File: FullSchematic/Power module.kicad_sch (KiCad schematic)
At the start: 1 part

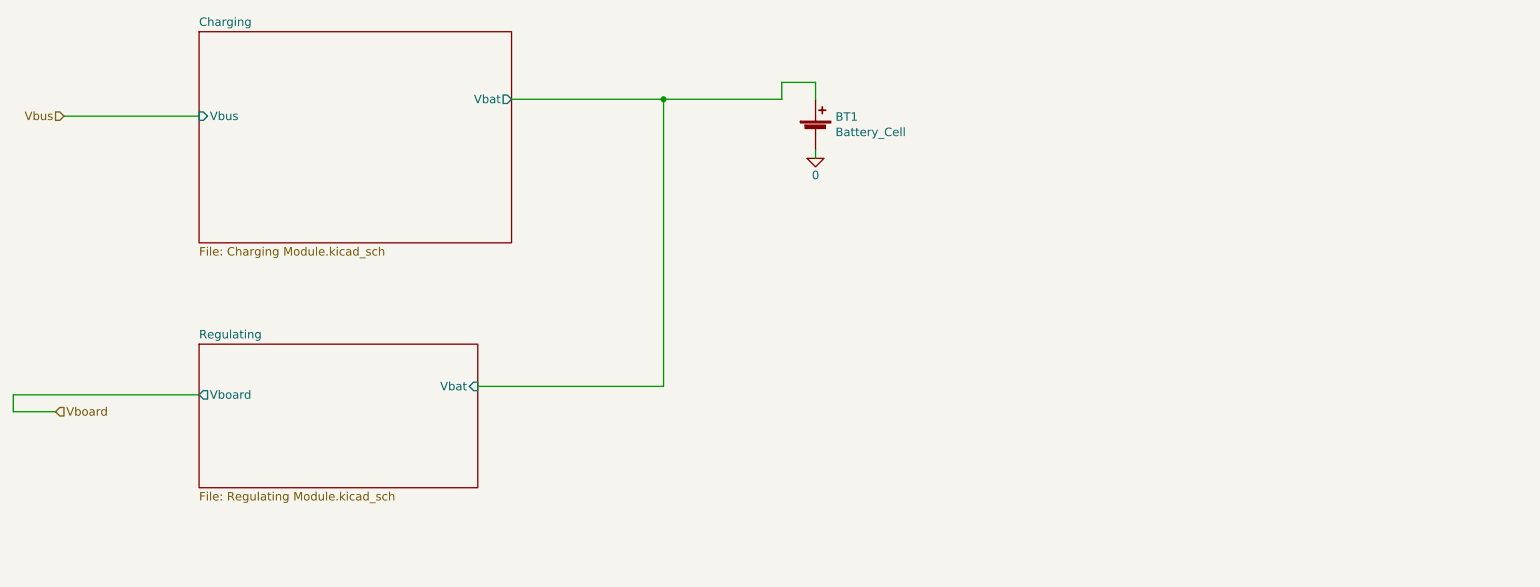
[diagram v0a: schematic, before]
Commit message: Added uvlo circuit
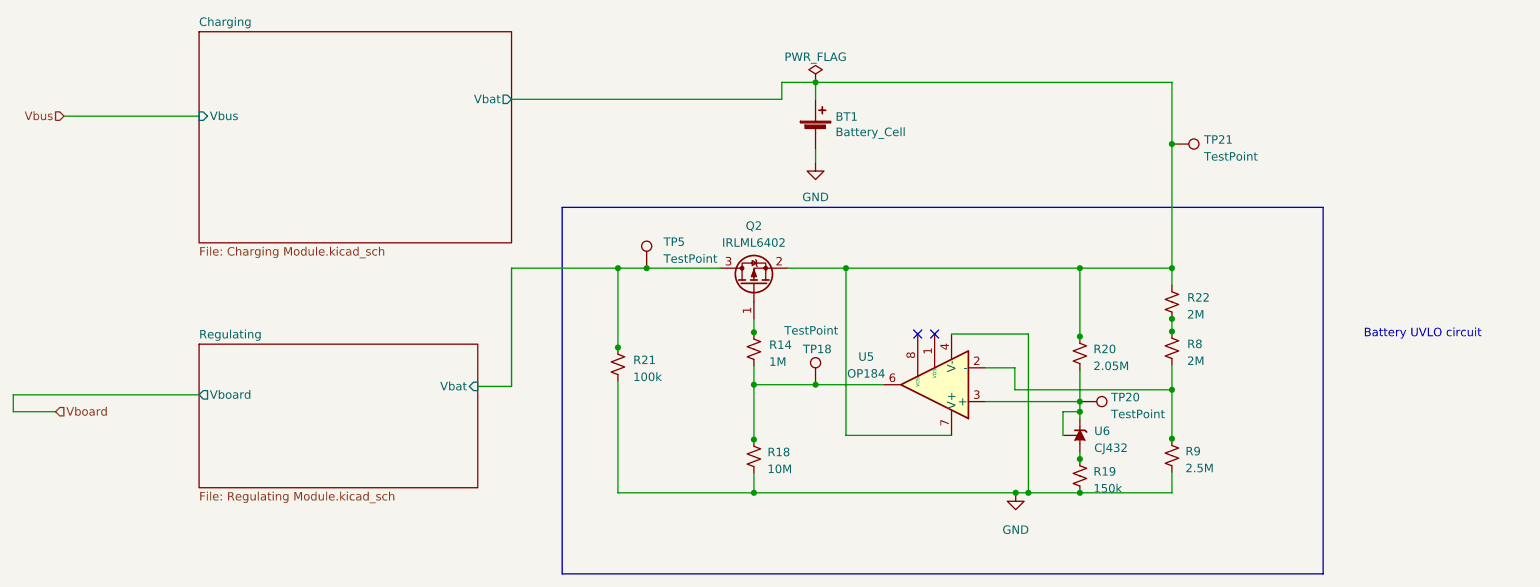
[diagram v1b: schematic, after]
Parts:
- added Q2: IRLML6402, Package_TO_SOT_SMD:SOT-23, symbol Transistor_FET:IRLML6402
- added R14: 1M, Resistor_SMD:R_0201_0603Metric, symbol Device:R_Small_US
- added R18: 10M, Resistor_SMD:R_0603_1608Metric_Pad0.98x0.95mm_HandSolder, symbol Device:R_Small_US
- added R19: 150k, Resistor_SMD:R_0603_1608Metric, symbol Device:R_Small_US
- added R20: 2.05M, Resistor_SMD:R_0603_1608Metric, symbol Device:R_Small_US
- added R21: 100k, Resistor_SMD:R_0201_0603Metric, symbol Device:R_Small_US
- added R22, R8: 2M, Resistor_SMD:R_0603_1608Metric, symbol Device:R_Small_US
- added R9: 2.5M, Resistor_SMD:R_1206_3216Metric, symbol Device:R_Small_US
- added TP18: TestPoint, TestPoint:TestPoint_Pad_D2.5mm, symbol Connector:TestPoint
- added TP20, TP21, TP5: TestPoint, TestPoint:TestPoint_Pad_D2.0mm, symbol Connector:TestPoint
- added U5: OP184, Library:SOIC127P600X175-8N, symbol Amplifier_Operational:OP07
- added U6: CJ432, Package_TO_SOT_SMD:SOT-23, symbol Reference_Voltage:CJ432
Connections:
- net Charging/Vbat: now also Q2.2 (S), R20.1, R22.1, TP21.1, U5.7 (V+)
- net 0 renamed GND
- net GND: now also R18.2, R19.2, R21.2, R9.2, U5.4 (V-)
- new net: R20.2, TP20.1, U5.3 (+), U6.1 (REF), U6.2 (K)
- new net: R8.2, R9.1, U5.2 (-)
- new net: R14.2, R18.1, TP18.1, U5.6
- new net: R22.2, R8.1
- new net: Q2.1 (G), R14.1
- new net: R19.1, U6.3 (A)
- new net Regulating/Vbat: Q2.3 (D), R21.1, TP5.1
- no-connect marks 0 -> 2

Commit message: Confirmed part numbers and prices
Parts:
- BT1: Populate (none) -> No
- Q2: JLCPCB Part # (none) -> C518785; Populate (none) -> Yes; Price (none) -> 0.05; Price ( 1 board) (none) -> 0.5; Price (5 boards) (none) -> 0.25
- R14: footprint Resistor_SMD:R_0201_0603Metric -> Resistor_SMD:R_0805_2012Metric; JLCPCB Part # (none) -> C416080; Populate (none) -> Yes; Price (none) -> 0.01; Price ( 1 board) (none) -> 0.01; Price (5 boards) (none) -> 0.05
- R18: footprint Resistor_SMD:R_0603_1608Metric_Pad0.98x0.95mm_HandSolder -> Resistor_SMD:R_0805_2012Metric; JLCPCB Part # (none) -> C26108; Populate (none) -> Yes; Price (none) -> 0.01; Price ( 1 board) (none) -> 0.01; Price (5 boards) (none) -> 0.05
- R19: footprint Resistor_SMD:R_0603_1608Metric -> Resistor_SMD:R_0402_1005Metric; JLCPCB Part # (none) -> C429049; Populate (none) -> Yes; Price (none) -> 0.01; Price ( 1 board) (none) -> 0.01; Price (5 boards) (none) -> 0.05
- R20: footprint Resistor_SMD:R_0603_1608Metric -> Resistor_SMD:R_0805_2012Metric; JLCPCB Part # (none) -> C784207; Populate (none) -> Yes; Price (none) -> 0.01; Price ( 1 board) (none) -> 0.01; Price (5 boards) (none) -> 0.05
- R21: footprint Resistor_SMD:R_0201_0603Metric -> Resistor_SMD:R_0805_2012Metric; JLCPCB Part # (none) -> C465471; Populate (none) -> Yes; Price (none) -> 0.01; Price ( 1 board) (none) -> 0.01; Price (5 boards) (none) -> 0.05
- R22, R8: JLCPCB Part # (none) -> C465466; Populate (none) -> Yes; Price (none) -> 0.01; Price ( 1 board) (none) -> 0.01; Price (5 boards) (none) -> 0.05
- R9: JLCPCB Part # (none) -> C508414; Populate (none) -> Yes; Price (none) -> 0.03; Price ( 1 board) (none) -> 0.03; Price (5 boards) (none) -> 0.15
- U5: JLCPCB Part # (none) -> C690879; Populate (none) -> Yes; Price (none) -> 3.17; Price ( 1 board) (none) -> 3.17; Price (5 boards) (none) -> 15.85
- U6: JLCPCB Part # (none) -> C8499; Populate (none) -> Yes; Price (none) -> 0.06; Price ( 1 board) (none) -> 0.06; Price (5 boards) (none) -> 0.3
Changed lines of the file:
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@@
+      (effects (font (size 1.27 1.27)) hide)
+    )
+    (property "Populate" "No" (at 154.94 81.28 0)
       (effects (font (size 1.27 1.27)) hide)
     )
@@
       (effects (font (size 1.27 1.27)) (justify left))
     )
-    (property "Footprint" "Resistor_SMD:R_0603_1608Metric" (at 194.691 114.427 0)
+    (property "Footprint" "Resistor_SMD:R_0805_2012Metric" (at 194.691 114.427 0)
       (effects (font (size 1.27 1.27)) hide)
     )
     (property "Datasheet" "~" (at 194.691 114.427 0)
+      (effects (font (size 1.27 1.27)) hide)
+    )
+    (property "JLCPCB Part #" "C784207" (at 194.691 114.427 0)
+      (effects (font (size 1.27 1.27)) hide)
+    )
+    (property "Populate" "Yes" (at 194.691 114.427 0)
+      (effects (font (size 1.27 1.27)) hide)
+    )
+    (property "Price" "0.01" (at 194.691 114.427 0)
+      (effects (font (size 1.27 1.27)) hide)
+    )
+    (property "Price ( 1 board)" "0.01" (at 194.691 114.427 0)
+      (effects (font (size 1.27 1.27)) hide)
+    )
+    (property "Price (5 boards)" "0.05" (at 194.691 114.427 0)
       (effects (font (size 1.27 1.27)) hide)
     )
@@
     )
     (property "Datasheet" "https://www.analog.com/media/en/technical-documentation/data-sheets/OP07.pdf" (at 171.577 122.936 0)
+      (effects (font (size 1.27 1.27)) hide)
+    )
+    (property "JLCPCB Part #" "C690879" (at 172.847 119.126 0)
+      (effects (font (size 1.27 1.27)) hide)
+    )
+    (property "Price" "3.17" (at 172.847 119.126 0)
+      (effects (font (size 1.27 1.27)) hide)
+    )
+    (property "Price ( 1 board)" "3.17" (at 172.847 119.126 0)
+      (effects (font (size 1.27 1.27)) hide)
+    )
+    (property "Price (5 boards)" "15.85" (at 172.847 119.126 0)
+      (effects (font (size 1.27 1.27)) hide)
+    )
+    (property "Populate" "Yes" (at 172.847 119.126 0)
       (effects (font (size 1.27 1.27)) hide)
     )
@@
       (effects (font (size 1.27 1.27)) hide)
     )
+    (property "JLCPCB Part #" "C465466" (at 208.534 106.68 0)
+      (effects (font (size 1.27 1.27)) hide)
+    )
+    (property "Populate" "Yes" (at 208.534 106.68 0)
+      (effects (font (size 1.27 1.27)) hide)
+    )
+    (property "Price" "0.01" (at 208.534 106.68 0)
+      (effects (font (size 1.27 1.27)) hide)
+    )
+    (property "Price ( 1 board)" "0.01" (at 208.534 106.68 0)
+      (effects (font (size 1.27 1.27)) hide)
+    )
+    (property "Price (5 boards)" "0.05" (at 208.534 106.68 0)
+      (effects (font (size 1.27 1.27)) hide)
+    )
     (pin "1")
     (pin "2")
@@
     )
     (property "Datasheet" "~" (at 208.534 129.794 0)
+      (effects (font (size 1.27 1.27)) hide)
+    )
+    (property "JLCPCB Part #" "C508414" (at 208.534 129.794 0)
+      (effects (font (size 1.27 1.27)) hide)
+    )
+    (property "Populate" "Yes" (at 208.534 129.794 0)
+      (effects (font (size 1.27 1.27)) hide)
+    )
+    (property "Price" "0.03" (at 208.534 129.794 0)
+      (effects (font (size 1.27 1.27)) hide)
+    )
+    (property "Price ( 1 board)" "0.03" (at 208.534 129.794 0)
+      (effects (font (size 1.27 1.27)) hide)
+    )
+    (property "Price (5 boards)" "0.15" (at 208.534 129.794 0)
       (effects (font (size 1.27 1.27)) hide)
     )
@@
       (effects (font (size 1.27 1.27)) (justify left) hide)
     )
+    (property "JLCPCB Part #" "C518785" (at 145.669 104.14 0)
+      (effects (font (size 1.27 1.27)) hide)
+    )
+    (property "Price" "0.05" (at 145.669 104.14 0)
+      (effects (font (size 1.27 1.27)) hide)
+    )
+    (property "Price ( 1 board)" "0.5" (at 145.669 104.14 0)
+      (effects (font (size 1.27 1.27)) hide)
+    )
+    (property "Price (5 boards)" "0.25" (at 145.669 104.14 0)
+      (effects (font (size 1.27 1.27)) hide)
+    )
+    (property "Populate" "Yes" (at 145.669 104.14 0)
+      (effects (font (size 1.27 1.27)) hide)
+    )
     (pin "1")
     (pin "2")
@@
       (effects (font (size 1.27 1.27) italic) hide)
     )
+    (property "JLCPCB Part #" "C8499" (at 194.691 126.746 0)
+      (effects (font (size 1.27 1.27)) hide)
+    )
+    (property "Price" "0.06" (at 194.691 126.746 0)
+      (effects (font (size 1.27 1.27)) hide)
+    )
+    (property "Price ( 1 board)" "0.06" (at 194.691 126.746 0)
+      (effects (font (size 1.27 1.27)) hide)
+    )
+    (property "Price (5 boards)" "0.3" (at 194.691 126.746 0)
+      (effects (font (size 1.27 1.27)) hide)
+    )
+    (property "Populate" "Yes" (at 194.691 126.746 0)
+      (effects (font (size 1.27 1.27)) hide)
+    )
     (pin "1")
     (pin "2")
@@
       (effects (font (size 1.27 1.27)) (justify left))
     )
-    (property "Footprint" "Resistor_SMD:R_0201_0603Metric" (at 145.669 113.792 0)
+    (property "Footprint" "Resistor_SMD:R_0805_2012Metric" (at 145.669 113.792 0)
       (effects (font (size 1.27 1.27)) hide)
     )
@@
       (effects (font (size 1.27 1.27)) hide)
     )
+    (property "JLCPCB Part #" "C416080" (at 145.669 113.792 0)
+      (effects (font (size 1.27 1.27)) hide)
+    )
+    (property "Populate" "Yes" (at 145.669 113.792 0)
+      (effects (font (size 1.27 1.27)) hide)
+    )
+    (property "Price" "0.01" (at 145.669 113.792 0)
+      (effects (font (size 1.27 1.27)) hide)
+    )
+    (property "Price ( 1 board)" "0.01" (at 145.669 113.792 0)
+      (effects (font (size 1.27 1.27)) hide)
+    )
+    (property "Price (5 boards)" "0.05" (at 145.669 113.792 0)
+      (effects (font (size 1.27 1.27)) hide)
+    )
     (pin "1")
     (pin "2")
@@
     )
     (property "Datasheet" "~" (at 208.534 113.665 0)
+      (effects (font (size 1.27 1.27)) hide)
+    )
+    (property "JLCPCB Part #" "C465466" (at 208.534 113.665 0)
+      (effects (font (size 1.27 1.27)) hide)
+    )
+    (property "Populate" "Yes" (at 208.534 113.665 0)
+      (effects (font (size 1.27 1.27)) hide)
+    )
+    (property "Price" "0.01" (at 208.534 113.665 0)
+      (effects (font (size 1.27 1.27)) hide)
+    )
+    (property "Price ( 1 board)" "0.01" (at 208.534 113.665 0)
+      (effects (font (size 1.27 1.27)) hide)
+    )
+    (property "Price (5 boards)" "0.05" (at 208.534 113.665 0)
       (effects (font (size 1.27 1.27)) hide)
     )
@@
       (effects (font (size 1.27 1.27)) (justify left))
     )
-    (property "Footprint" "Resistor_SMD:R_0201_0603Metric" (at 125.222 116.078 0)
+    (property "Footprint" "Resistor_SMD:R_0805_2012Metric" (at 125.222 116.078 0)
       (effects (font (size 1.27 1.27)) hide)
     )
@@
       (effects (font (size 1.27 1.27)) hide)
     )
+    (property "JLCPCB Part #" "C465471" (at 125.222 116.078 0)
+      (effects (font (size 1.27 1.27)) hide)
+    )
+    (property "Populate" "Yes" (at 125.222 116.078 0)
+      (effects (font (size 1.27 1.27)) hide)
+    )
+    (property "Price" "0.01" (at 125.222 116.078 0)
+      (effects (font (size 1.27 1.27)) hide)
+    )
+    (property "Price ( 1 board)" "0.01" (at 125.222 116.078 0)
+      (effects (font (size 1.27 1.27)) hide)
+    )
+    (property "Price (5 boards)" "0.05" (at 125.222 116.078 0)
+      (effects (font (size 1.27 1.27)) hide)
+    )
     (pin "1")
     (pin "2")
@@
       (effects (font (size 1.27 1.27)) (justify left))
     )
-    (property "Footprint" "Resistor_SMD:R_0603_1608Metric" (at 194.691 132.842 0)
+    (property "Footprint" "Resistor_SMD:R_0402_1005Metric" (at 194.691 132.842 0)
       (effects (font (size 1.27 1.27)) hide)
     )
@@
       (effects (font (size 1.27 1.27)) hide)
     )
+    (property "JLCPCB Part #" "C429049" (at 194.691 132.842 0)
+      (effects (font (size 1.27 1.27)) hide)
+    )
+    (property "Populate" "Yes" (at 194.691 132.842 0)
+      (effects (font (size 1.27 1.27)) hide)
+    )
+    (property "Price" "0.01" (at 194.691 132.842 0)
+      (effects (font (size 1.27 1.27)) hide)
+    )
+    (property "Price ( 1 board)" "0.01" (at 194.691 132.842 0)
+      (effects (font (size 1.27 1.27)) hide)
+    )
+    (property "Price (5 boards)" "0.05" (at 194.691 132.842 0)
+      (effects (font (size 1.27 1.27)) hide)
+    )
     (pin "1")
     (pin "2")
@@
       (effects (font (size 1.27 1.27)) (justify left))
     )
-    (property "Footprint" "Resistor_SMD:R_0603_1608Metric_Pad0.98x0.95mm_HandSolder" (at 145.669 129.921 0)
+    (property "Footprint" "Resistor_SMD:R_0805_2012Metric" (at 145.669 129.921 0)
       (effects (font (size 1.27 1.27)) hide)
     )
@@
       (effects (font (size 1.27 1.27)) hide)
     )
+    (property "JLCPCB Part #" "C26108" (at 145.669 129.921 0)
+      (effects (font (size 1.27 1.27)) hide)
+    )
+    (property "Populate" "Yes" (at 145.669 129.921 0)
+      (effects (font (size 1.27 1.27)) hide)
+    )
+    (property "Price" "0.01" (at 145.669 129.921 0)
+      (effects (font (size 1.27 1.27)) hide)
+    )
+    (property "Price ( 1 board)" "0.01" (at 145.669 129.921 0)
+      (effects (font (size 1.27 1.27)) hide)
+    )
+    (property "Price (5 boards)" "0.05" (at 145.669 129.921 0)
+      (effects (font (size 1.27 1.27)) hide)
+    )

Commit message: corrected connection
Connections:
- net GND: no longer R18.2
- net at R19.1, U6.3 (A): now also R18.2
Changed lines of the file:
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@@
   (junction (at 145.669 111.252) (diameter 0) (color 0 0 0 0)
-  )
-  (junction (at 145.669 135.382) (diameter 0) (color 0 0 0 0)
   )
   (junction (at 194.691 121.666) (diameter 0) (color 0 0 0 0)
@@
     (stroke (width 0) (type default))
   )
-  (wire (pts (xy 145.669 135.382) (xy 185.039 135.382))
-    (stroke (width 0) (type default))
-  )
   (wire (pts (xy 186.944 111.506) (xy 186.944 135.382))
     (stroke (width 0) (type default))
@@
     (stroke (width 0) (type default))
   )
+  (wire (pts (xy 192.278 132.461) (xy 192.278 130.302))
+    (stroke (width 0) (type default))
+  )
   (wire (pts (xy 149.86 73.66) (xy 154.94 73.66))
     (stroke (width 0) (type default))
@@
     (stroke (width 0) (type default))
   )
+  (wire (pts (xy 192.278 130.302) (xy 194.691 130.302))
+    (stroke (width 0) (type default))
+  )
   (wire (pts (xy 208.534 132.334) (xy 208.534 135.382))
     (stroke (width 0) (type default))
@@
     (stroke (width 0) (type default))
   )
-  (wire (pts (xy 145.669 132.461) (xy 145.669 135.382))
-    (stroke (width 0) (type default))
-  )
   (wire (pts (xy 175.387 126.746) (xy 159.512 126.746))
     (stroke (width 0) (type default))
@@
     (stroke (width 0) (type default))
   )
-  (wire (pts (xy 125.222 135.382) (xy 145.669 135.382))
+  (wire (pts (xy 125.222 135.382) (xy 185.039 135.382))
     (stroke (width 0) (type default))
   )
@@
     (stroke (width 0) (type default))
   )
+  (wire (pts (xy 145.669 132.461) (xy 192.278 132.461))
+    (stroke (width 0) (type default))
+  )

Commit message: Checked part #s, prices, footprints
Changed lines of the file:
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@@
     (effects (font (size 1.27 1.27)) (justify left top))
   )
-  (hierarchical_label "Vboard" (shape input) (at 40.64 123.19 0) (fields_autoplaced)
+  (hierarchical_label "Vboard" (shape output) (at 40.64 123.19 0) (fields_autoplaced)
     (effects (font (size 1.27 1.27)) (justify left))
   )

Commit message: generated files
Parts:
- BT1: JLCPCB Part # C2988620 -> (none)
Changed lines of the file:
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@@
       (effects (font (size 1.27 1.27)) hide)
     )
-    (property "JLCPCB Part #" "C2988620" (at 154.94 81.28 0)
+    (property "JLCPCB Part #" "" (at 154.94 81.28 0)
       (effects (font (size 1.27 1.27)) hide)
     )
